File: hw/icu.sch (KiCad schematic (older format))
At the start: 4 parts, among them J101 AMPSEAL_8_POS_VERT_BLACK_SEAL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, J102 AMPSEAL_23_POS_VERT_GRAY_SEAL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

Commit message: implementing icu in CM_6.2.1
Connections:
- net Power supply/GND: now also J101.7 (S), J101.8 (S)
- net Power supply/VIN: no longer J101.6 (S)
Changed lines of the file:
@@
 Connection ~ 1650 2100
 Wire Wire Line
-	1650 2850 1450 2850
-Connection ~ 1650 2400
-Wire Wire Line
-	1450 2250 2850 2250
+	1450 2250 1750 2250
 Wire Wire Line
 	2850 2250 2850 2800
@@
 Wire Wire Line
 	1650 2100 3200 2100
-Wire Wire Line
-	1650 2400 1650 2850
 $Comp
 L icu-rescue:VDD #PWR0101
@@
 Wire Wire Line
 	7200 5750 5950 5750
+Wire Wire Line
+	1450 3000 1750 3000
+Wire Wire Line
+	1750 3000 1750 2250
+Connection ~ 1750 2250
+Wire Wire Line
+	1750 2250 2850 2250
+Wire Wire Line
+	1750 3000 1750 3150
+Wire Wire Line
+	1750 3150 1450 3150
+Connection ~ 1750 3000
 $EndSCHEMATC

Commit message: CM_6.2.1 delivered, first customer machine with CCU, HCU & ICU
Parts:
- removed R101: 120, yageo:0603, symbol yageo:120
- F101: symbol icu-rescue:FUSE_MC36211_350MA -> FUSE_MC36211_350MA
- J101: symbol icu-rescue:AMPSEAL_8_POS_VERT_BLACK_SEALED_1-776276-1 -> AMPSEAL_8_POS_VERT_BLACK_SEALED_1-776276-1
- J102: symbol icu-rescue:AMPSEAL_23_POS_VERT_GRAY_SEALED_1-776228-4 -> AMPSEAL_23_POS_VERT_GRAY_SEALED_1-776228-4
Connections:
- net labels added: 5V_OUT
- net labels removed: VDD_OUT
- wire segments 120 -> 109

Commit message: 050518: Kikepera head prototype first revision, saw not working
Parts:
- F101: symbol FUSE_MC36211_350MA -> icu-rescue:FUSE_MC36211_350MA
- J101: symbol AMPSEAL_8_POS_VERT_BLACK_SEALED_1-776276-1 -> icu-rescue:AMPSEAL_8_POS_VERT_BLACK_SEALED_1-776276-1
- J102: symbol AMPSEAL_23_POS_VERT_GRAY_SEALED_1-776228-4 -> icu-rescue:AMPSEAL_23_POS_VERT_GRAY_SEALED_1-776228-4
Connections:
- wire segments 109 -> 111
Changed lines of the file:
@@
-EESchema Schematic File Version 2
-LIBS:kemet
-LIBS:usevolt
-LIBS:wurth_elektronik_LED
-LIBS:power
-LIBS:yageo
+EESchema Schematic File Version 4
 LIBS:icu-cache
 EELAYER 26 0
@@
 $EndSheet
 $Comp
-L +3V3 #PWR01
+L icu-rescue:+3V3 #PWR01
 U 1 1 57E93CBF
 P 4900 2050
@@
 $EndComp
 $Comp
-L VDD #PWR02
+L icu-rescue:VDD #PWR02
 U 1 1 57E93E22
 P 4400 2050
@@
 $EndComp
 $Comp
-L +5V #PWR03
+L icu-rescue:+5V #PWR03
 U 1 1 589766AF
 P 4650 2050
@@
 	4650 2250 4300 2250
 $Comp
-L AMPSEAL_8_POS_VERT_BLACK_SEALED_1-776276-1 J101
+L icu-rescue:AMPSEAL_8_POS_VERT_BLACK_SEALED_1-776276-1 J101
 U 1 1 5A79A3F3
 P 1350 2100
@@
 $EndComp
 $Comp
-L AMPSEAL_8_POS_VERT_BLACK_SEALED_1-776276-1 J101
+L icu-rescue:AMPSEAL_8_POS_VERT_BLACK_SEALED_1-776276-1 J101
 U 2 1 5A79A545
 P 1350 2250
@@
 $EndComp
 $Comp
-L AMPSEAL_8_POS_VERT_BLACK_SEALED_1-776276-1 J101
+L icu-rescue:AMPSEAL_8_POS_VERT_BLACK_SEALED_1-776276-1 J101
 U 3 1 5A79A8B7
 P 1350 2400
@@
 $EndComp
 $Comp
-L AMPSEAL_8_POS_VERT_BLACK_SEALED_1-776276-1 J101
+L icu-rescue:AMPSEAL_8_POS_VERT_BLACK_SEALED_1-776276-1 J101
 U 4 1 5A79A9C7
 P 1350 2550
@@
 $EndComp
 $Comp
-L AMPSEAL_8_POS_VERT_BLACK_SEALED_1-776276-1 J101
+L icu-rescue:AMPSEAL_8_POS_VERT_BLACK_SEALED_1-776276-1 J101
 U 5 1 5A79AADD
 P 1350 2700
@@
 $EndComp
 $Comp
-L AMPSEAL_8_POS_VERT_BLACK_SEALED_1-776276-1 J101
+L icu-rescue:AMPSEAL_8_POS_VERT_BLACK_SEALED_1-776276-1 J101
 U 6 1 5A79AD45
 P 1350 2850
@@
 $EndComp
 $Comp
-L AMPSEAL_8_POS_VERT_BLACK_SEALED_1-776276-1 J101
+L icu-rescue:AMPSEAL_8_POS_VERT_BLACK_SEALED_1-776276-1 J101
 U 7 1 5A79AE65
 P 1350 3000
@@
 $EndComp
 $Comp
-L AMPSEAL_8_POS_VERT_BLACK_SEALED_1-776276-1 J101
+L icu-rescue:AMPSEAL_8_POS_VERT_BLACK_SEALED_1-776276-1 J101
 U 8 1 5A79AF81
 P 1350 3150
@@
 $EndComp
 Wire Wire Line
-	1450 2100 3200 2100
+	1450 2100 1650 2100
 Wire Wire Line
 	1450 2400 1650 2400
 Wire Wire Line
-	1650 2100 1650 2850
+	1650 2100 1650 2400
 Connection ~ 1650 2100
 Wire Wire Line
@@
 	5800 4550 7200 4550
 $Comp
-L AMPSEAL_23_POS_VERT_GRAY_SEALED_1-776228-4 J102
+L icu-rescue:AMPSEAL_23_POS_VERT_GRAY_SEALED_1-776228-4 J102
 U 1 1 5A7B0192
 P 4600 5050
@@
 $EndComp
 $Comp
-L AMPSEAL_23_POS_VERT_GRAY_SEALED_1-776228-4 J102
+L icu-rescue:AMPSEAL_23_POS_VERT_GRAY_SEALED_1-776228-4 J102
 U 2 1 5A7B0214
 P 4600 5150
@@
 $EndComp
 $Comp
-L AMPSEAL_23_POS_VERT_GRAY_SEALED_1-776228-4 J102
+L icu-rescue:AMPSEAL_23_POS_VERT_GRAY_SEALED_1-776228-4 J102
 U 3 1 5A7B037A
 P 4600 5250
@@
 $EndComp
 $Comp
-L AMPSEAL_23_POS_VERT_GRAY_SEALED_1-776228-4 J102
+L icu-rescue:AMPSEAL_23_POS_VERT_GRAY_SEALED_1-776228-4 J102
 U 4 1 5A7B03F0
 P 4600 5350
@@
 $EndComp
 $Comp
-L AMPSEAL_23_POS_VERT_GRAY_SEALED_1-776228-4 J102
+L icu-rescue:AMPSEAL_23_POS_VERT_GRAY_SEALED_1-776228-4 J102
 U 5 1 5A7B0464
 P 4600 5600
@@
 $EndComp
 $Comp
-L AMPSEAL_23_POS_VERT_GRAY_SEALED_1-776228-4 J102
+L icu-rescue:AMPSEAL_23_POS_VERT_GRAY_SEALED_1-776228-4 J102
 U 6 1 5A7B04DA
 P 4600 6000
@@
 $EndComp
 $Comp
-L AMPSEAL_23_POS_VERT_GRAY_SEALED_1-776228-4 J102
+L icu-rescue:AMPSEAL_23_POS_VERT_GRAY_SEALED_1-776228-4 J102
 U 7 1 5A7B0552
 P 4600 6400
@@
 $EndComp
 $Comp
-L AMPSEAL_23_POS_VERT_GRAY_SEALED_1-776228-4 J102
+L icu-rescue:AMPSEAL_23_POS_VERT_GRAY_SEALED_1-776228-4 J102
 U 8 1 5A7B05CC
 P 4600 6800
@@
 $EndComp
 $Comp
-L AMPSEAL_23_POS_VERT_GRAY_SEALED_1-776228-4 J102
+L icu-rescue:AMPSEAL_23_POS_VERT_GRAY_SEALED_1-776228-4 J102
 U 9 1 5A7B0648
 P 12750 3600
@@
 $EndComp
 $Comp
-L AMPSEAL_23_POS_VERT_GRAY_SEALED_1-776228-4 J102
+L icu-rescue:AMPSEAL_23_POS_VERT_GRAY_SEALED_1-776228-4 J102
 U 10 1 5A7B075E
 P 12750 4200
@@
 $EndComp
 $Comp
-L AMPSEAL_23_POS_VERT_GRAY_SEALED_1-776228-4 J102
+L icu-rescue:AMPSEAL_23_POS_VERT_GRAY_SEALED_1-776228-4 J102
 U 11 1 5A7B07EA
 P 12750 4800
@@
 $EndComp
 $Comp
-L AMPSEAL_23_POS_VERT_GRAY_SEALED_1-776228-4 J102
+L icu-rescue:AMPSEAL_23_POS_VERT_GRAY_SEALED_1-776228-4 J102
 U 12 1 5A7B086C
 P 12750 5400
@@
 $EndComp
 $Comp
-L AMPSEAL_23_POS_VERT_GRAY_SEALED_1-776228-4 J102
+L icu-rescue:AMPSEAL_23_POS_VERT_GRAY_SEALED_1-776228-4 J102
 U 13 1 5A7B08F0
 P 12750 6000
@@
 $EndComp
 $Comp
-L AMPSEAL_23_POS_VERT_GRAY_SEALED_1-776228-4 J102
+L icu-rescue:AMPSEAL_23_POS_VERT_GRAY_SEALED_1-776228-4 J102
 U 14 1 5A7B0976
 P 12750 6600
@@
 $EndComp
 $Comp
-L AMPSEAL_23_POS_VERT_GRAY_SEALED_1-776228-4 J102
+L icu-rescue:AMPSEAL_23_POS_VERT_GRAY_SEALED_1-776228-4 J102
 U 15 1 5A7B09FE
 P 12750 7200
@@
 $EndComp
 $Comp
-L AMPSEAL_23_POS_VERT_GRAY_SEALED_1-776228-4 J102
+L icu-rescue:AMPSEAL_23_POS_VERT_GRAY_SEALED_1-776228-4 J102
 U 16 1 5A7B0A88
 P 12750 3800
@@
 $EndComp
 $Comp
-L AMPSEAL_23_POS_VERT_GRAY_SEALED_1-776228-4 J102
+L icu-rescue:AMPSEAL_23_POS_VERT_GRAY_SEALED_1-776228-4 J102
 U 17 1 5A7B0B14
 P 12750 4400
@@
 $EndComp
 $Comp
-L AMPSEAL_23_POS_VERT_GRAY_SEALED_1-776228-4 J102
+L icu-rescue:AMPSEAL_23_POS_VERT_GRAY_SEALED_1-776228-4 J102
 U 18 1 5A7B0C28
 P 12750 5000
@@
 $EndComp
 $Comp
-L AMPSEAL_23_POS_VERT_GRAY_SEALED_1-776228-4 J102
+L icu-rescue:AMPSEAL_23_POS_VERT_GRAY_SEALED_1-776228-4 J102
 U 19 1 5A7B0CB4
 P 12750 5600
@@
 $EndComp
 $Comp
-L AMPSEAL_23_POS_VERT_GRAY_SEALED_1-776228-4 J102
+L icu-rescue:AMPSEAL_23_POS_VERT_GRAY_SEALED_1-776228-4 J102
 U 20 1 5A7B0DD2
 P 12750 6200
@@
 $EndComp
 $Comp
-L AMPSEAL_23_POS_VERT_GRAY_SEALED_1-776228-4 J102
+L icu-rescue:AMPSEAL_23_POS_VERT_GRAY_SEALED_1-776228-4 J102
 U 21 1 5A7B0F0C
 P 12750 6800
@@
 $EndComp
 $Comp
-L AMPSEAL_23_POS_VERT_GRAY_SEALED_1-776228-4 J102
+L icu-rescue:AMPSEAL_23_POS_VERT_GRAY_SEALED_1-776228-4 J102
 U 22 1 5A7B0FA2
 P 12750 7400
@@
 $EndComp
 $Comp
-L AMPSEAL_23_POS_VERT_GRAY_SEALED_1-776228-4 J102
+L icu-rescue:AMPSEAL_23_POS_VERT_GRAY_SEALED_1-776228-4 J102
 U 23 1 5A7B103A
 P 1700 5850
@@
 	12450 4200 12650 4200
 $Comp
-L FUSE_MC36211_350MA F101
+L icu-rescue:FUSE_MC36211_350MA F101
 U 1 1 5A7D8C08
 P 2400 5850
@@
 5V_OUT
 $Comp
-L +5V #PWR04
+L icu-rescue:+5V #PWR04
 U 1 1 5A7DBD62
 P 2800 5650
@@
 Wire Wire Line
 	6000 6800 7200 6800
+Wire Wire Line
+	1650 2100 3200 2100
+Wire Wire Line
+	1650 2400 1650 2850
 $EndSCHEMATC

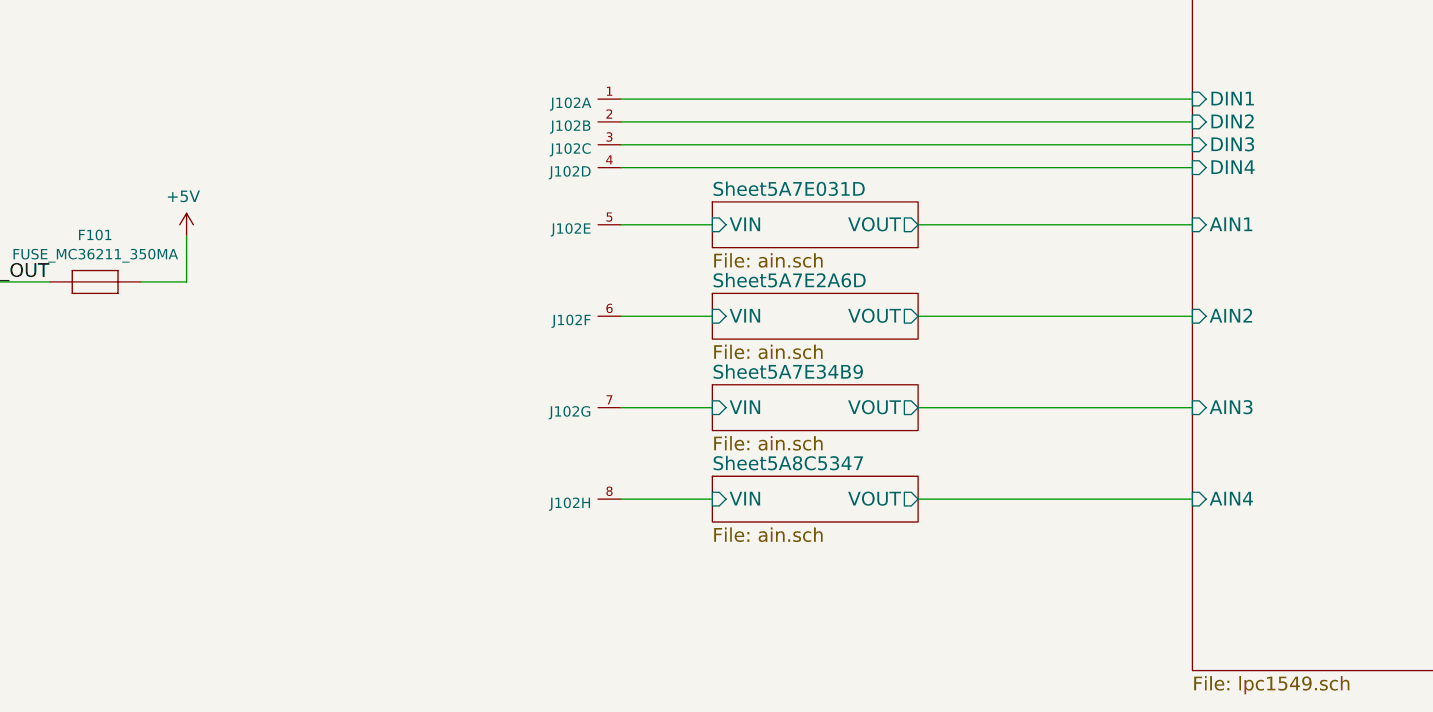
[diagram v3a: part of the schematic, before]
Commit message: analog inputs replaced with digital inputs
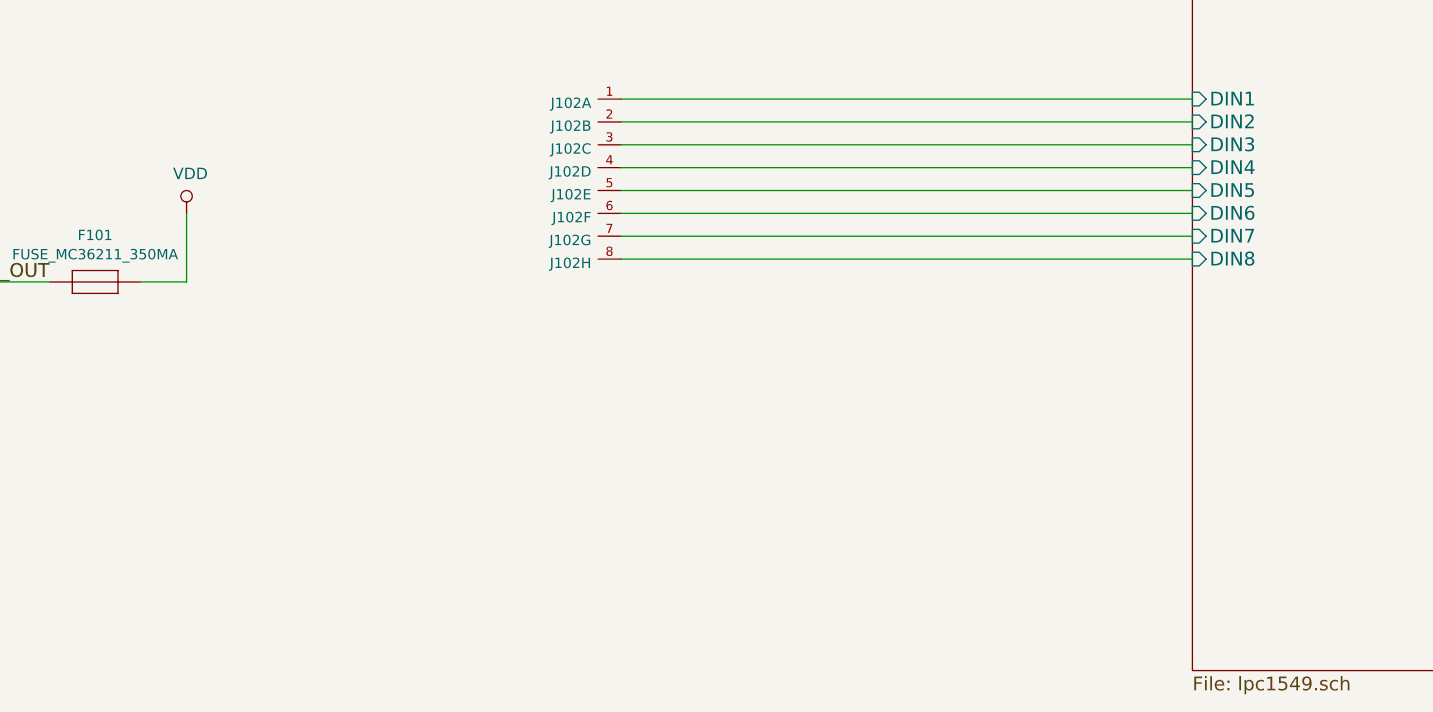
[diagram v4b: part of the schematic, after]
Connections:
- net +5V: no longer F101.P$1
- net VDD: now also F101.P$1
- net Sheet5A7E031D/VIN renamed lpc1549/DIN5
- net Sheet5A7E2A6D/VIN renamed lpc1549/DIN6
- net Sheet5A7E34B9/VIN renamed lpc1549/DIN7
- net Sheet5A8C5347/VIN renamed lpc1549/DIN8
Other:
- moved on the sheet: J102E, J102F, J102G, J102H
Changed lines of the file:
@@
 $Descr A3 16535 11693
 encoding utf-8
-Sheet 1 14
+Sheet 1 10
 Title "ESB version 1"
 Date "2017-02-02"
@@
 L icu-rescue:AMPSEAL_23_POS_VERT_GRAY_SEALED_1-776228-4 J102
 U 5 1 5A7B0464
-P 4600 5600
-F 0 "J102" H 4629 5582 45  0000 L CNN
-F 1 "AMPSEAL_23_POS_VERT_GRAY_SEALED_1-776228-4" H 4600 5600 45  0001 L BNN
-F 2 "usevolt:AMPSEAL_23_POS_776200-1" H 4630 5750 20  0001 C CNN
-F 3 "http://www.mouser.com/ds/2/418/NG_CD_776228_C13-672564.pdf" H 4700 5570 60  0001 C CNN
-F 4 "571-1-776228-4" H 5100 5970 60  0001 C CNN "1st Source Part Number"
-F 5 "1-776228-4" H 4900 5770 60  0001 C CNN "Manufacturer Part Number"
-F 6 "Mouser" H 5000 5870 60  0001 C CNN "1st Source"
-F 7 "TE Connectivity" H 4800 5670 60  0001 C CNN "Manufacturer"
-	5    4600 5600
+P 4600 5450
+F 0 "J102" H 4629 5432 45  0000 L CNN
+F 1 "AMPSEAL_23_POS_VERT_GRAY_SEALED_1-776228-4" H 4600 5450 45  0001 L BNN
+F 2 "usevolt:AMPSEAL_23_POS_776200-1" H 4630 5600 20  0001 C CNN
+F 3 "http://www.mouser.com/ds/2/418/NG_CD_776228_C13-672564.pdf" H 4700 5420 60  0001 C CNN
+F 4 "571-1-776228-4" H 5100 5820 60  0001 C CNN "1st Source Part Number"
+F 5 "1-776228-4" H 4900 5620 60  0001 C CNN "Manufacturer Part Number"
+F 6 "Mouser" H 5000 5720 60  0001 C CNN "1st Source"
+F 7 "TE Connectivity" H 4800 5520 60  0001 C CNN "Manufacturer"
+	5    4600 5450
 	-1   0    0    -1
 $EndComp
@@
 L icu-rescue:AMPSEAL_23_POS_VERT_GRAY_SEALED_1-776228-4 J102
 U 6 1 5A7B04DA
-P 4600 6000
-F 0 "J102" H 4629 5982 45  0000 L CNN
-F 1 "AMPSEAL_23_POS_VERT_GRAY_SEALED_1-776228-4" H 4600 6000 45  0001 L BNN
-F 2 "usevolt:AMPSEAL_23_POS_776200-1" H 4630 6150 20  0001 C CNN
-F 3 "http://www.mouser.com/ds/2/418/NG_CD_776228_C13-672564.pdf" H 4700 5970 60  0001 C CNN
-F 4 "571-1-776228-4" H 5100 6370 60  0001 C CNN "1st Source Part Number"
-F 5 "1-776228-4" H 4900 6170 60  0001 C CNN "Manufacturer Part Number"
-F 6 "Mouser" H 5000 6270 60  0001 C CNN "1st Source"
-F 7 "TE Connectivity" H 4800 6070 60  0001 C CNN "Manufacturer"
-	6    4600 6000
+P 4600 5550
+F 0 "J102" H 4629 5532 45  0000 L CNN
+F 1 "AMPSEAL_23_POS_VERT_GRAY_SEALED_1-776228-4" H 4600 5550 45  0001 L BNN
+F 2 "usevolt:AMPSEAL_23_POS_776200-1" H 4630 5700 20  0001 C CNN
+F 3 "http://www.mouser.com/ds/2/418/NG_CD_776228_C13-672564.pdf" H 4700 5520 60  0001 C CNN
+F 4 "571-1-776228-4" H 5100 5920 60  0001 C CNN "1st Source Part Number"
+F 5 "1-776228-4" H 4900 5720 60  0001 C CNN "Manufacturer Part Number"
+F 6 "Mouser" H 5000 5820 60  0001 C CNN "1st Source"
+F 7 "TE Connectivity" H 4800 5620 60  0001 C CNN "Manufacturer"
+	6    4600 5550
 	-1   0    0    -1
 $EndComp
@@
 L icu-rescue:AMPSEAL_23_POS_VERT_GRAY_SEALED_1-776228-4 J102
 U 7 1 5A7B0552
-P 4600 6400
-F 0 "J102" H 4629 6382 45  0000 L CNN
-F 1 "AMPSEAL_23_POS_VERT_GRAY_SEALED_1-776228-4" H 4600 6400 45  0001 L BNN
-F 2 "usevolt:AMPSEAL_23_POS_776200-1" H 4630 6550 20  0001 C CNN
-F 3 "http://www.mouser.com/ds/2/418/NG_CD_776228_C13-672564.pdf" H 4700 6370 60  0001 C CNN
-F 4 "571-1-776228-4" H 5100 6770 60  0001 C CNN "1st Source Part Number"
-F 5 "1-776228-4" H 4900 6570 60  0001 C CNN "Manufacturer Part Number"
-F 6 "Mouser" H 5000 6670 60  0001 C CNN "1st Source"
-F 7 "TE Connectivity" H 4800 6470 60  0001 C CNN "Manufacturer"
-	7    4600 6400
+P 4600 5650
+F 0 "J102" H 4629 5632 45  0000 L CNN
+F 1 "AMPSEAL_23_POS_VERT_GRAY_SEALED_1-776228-4" H 4600 5650 45  0001 L BNN
+F 2 "usevolt:AMPSEAL_23_POS_776200-1" H 4630 5800 20  0001 C CNN
+F 3 "http://www.mouser.com/ds/2/418/NG_CD_776228_C13-672564.pdf" H 4700 5620 60  0001 C CNN
+F 4 "571-1-776228-4" H 5100 6020 60  0001 C CNN "1st Source Part Number"
+F 5 "1-776228-4" H 4900 5820 60  0001 C CNN "Manufacturer Part Number"
+F 6 "Mouser" H 5000 5920 60  0001 C CNN "1st Source"
+F 7 "TE Connectivity" H 4800 5720 60  0001 C CNN "Manufacturer"
+	7    4600 5650
 	-1   0    0    -1
 $EndComp
@@
 L icu-rescue:AMPSEAL_23_POS_VERT_GRAY_SEALED_1-776228-4 J102
 U 8 1 5A7B05CC
-P 4600 6800
-F 0 "J102" H 4629 6782 45  0000 L CNN
-F 1 "AMPSEAL_23_POS_VERT_GRAY_SEALED_1-776228-4" H 4600 6800 45  0001 L BNN
-F 2 "usevolt:AMPSEAL_23_POS_776200-1" H 4630 6950 20  0001 C CNN
-F 3 "http://www.mouser.com/ds/2/418/NG_CD_776228_C13-672564.pdf" H 4700 6770 60  0001 C CNN
-F 4 "571-1-776228-4" H 5100 7170 60  0001 C CNN "1st Source Part Number"
-F 5 "1-776228-4" H 4900 6970 60  0001 C CNN "Manufacturer Part Number"
-F 6 "Mouser" H 5000 7070 60  0001 C CNN "1st Source"
-F 7 "TE Connectivity" H 4800 6870 60  0001 C CNN "Manufacturer"
-	8    4600 6800
+P 4600 5750
+F 0 "J102" H 4629 5732 45  0000 L CNN
+F 1 "AMPSEAL_23_POS_VERT_GRAY_SEALED_1-776228-4" H 4600 5750 45  0001 L BNN
+F 2 "usevolt:AMPSEAL_23_POS_776200-1" H 4630 5900 20  0001 C CNN
+F 3 "http://www.mouser.com/ds/2/418/NG_CD_776228_C13-672564.pdf" H 4700 5720 60  0001 C CNN
+F 4 "571-1-776228-4" H 5100 6120 60  0001 C CNN "1st Source Part Number"
+F 5 "1-776228-4" H 4900 5920 60  0001 C CNN "Manufacturer Part Number"
+F 6 "Mouser" H 5000 6020 60  0001 C CNN "1st Source"
+F 7 "TE Connectivity" H 4800 5820 60  0001 C CNN "Manufacturer"
+	8    4600 5750
 	-1   0    0    -1
 $EndComp
@@
 F26 "DIN2" I L 7200 5150 60
 F27 "DIN3" I L 7200 5250 60
-F28 "AIN1" I L 7200 5600 60
-F29 "AIN2" I L 7200 6000 60
-F30 "AIN3" I L 7200 6400 60
-F31 "AIN4" I L 7200 6800 60
-F32 "DIN4" I L 7200 5350 60
+F28 "DIN4" I L 7200 5350 60
+F29 "DIN5" I L 7200 5450 60
+F30 "DIN6" I L 7200 5550 60
+F31 "DIN7" I L 7200 5650 60
+F32 "DIN8" I L 7200 5750 60
 $EndSheet
 Wire Wire Line
@@
 Text Label 2200 5850 2    60   ~ 0
 5V_OUT
-$Comp
-L icu-rescue:+5V #PWR04
-U 1 1 5A7DBD62
-P 2800 5650
-F 0 "#PWR04" H 2800 5500 50  0001 C CNN
-F 1 "+5V" H 2815 5823 50  0000 C CNN
-F 2 "" H 2800 5650 50  0000 C CNN
-F 3 "" H 2800 5650 50  0000 C CNN
-	1    2800 5650
-	-1   0    0    -1
-$EndComp
-Wire Wire Line
-	2800 5650 2800 5850
 Wire Wire Line
 	2800 5850 2600 5850
-$Sheet
-S 5100 5500 900  200
-U 5A7E031E
-F0 "Sheet5A7E031D" 60
-F1 "ain.sch" 60
-F2 "VOUT" O R 6000 5600 60
-F3 "VIN" I L 5100 5600 60
-$EndSheet
-$Sheet
-S 5100 5900 900  200
-U 5A7E2A6E
-F0 "Sheet5A7E2A6D" 60
-F1 "ain.sch" 60
-F2 "VOUT" O R 6000 6000 60
-F3 "VIN" I L 5100 6000 60
-$EndSheet
-$Sheet
-S 5100 6300 900  200
-U 5A7E34BA
-F0 "Sheet5A7E34B9" 60
-F1 "ain.sch" 60
-F2 "VOUT" O R 6000 6400 60
-F3 "VIN" I L 5100 6400 60
-$EndSheet
-Wire Wire Line
-	4700 5600 5100 5600
-Wire Wire Line
-	5100 6000 4700 6000
-Wire Wire Line
-	4700 6400 5100 6400
 Wire Wire Line
 	4700 5050 7200 5050
@@
 	4700 5250 7200 5250
 Wire Wire Line
-	7200 6400 6000 6400
-Wire Wire Line
-	6000 6000 7200 6000
-Wire Wire Line
-	7200 5600 6000 5600
-$Sheet
-S 5100 6700 900  200
-U 5A8C5348
-F0 "Sheet5A8C5347" 60
-F1 "ain.sch" 60
-F2 "VOUT" O R 6000 6800 60
-F3 "VIN" I L 5100 6800 60
-$EndSheet
-Wire Wire Line
-	5100 6800 4700 6800
-Wire Wire Line
 	7200 5350 4700 5350
 Wire Wire Line
-	6000 6800 7200 6800
-Wire Wire Line
 	1650 2100 3200 2100
 Wire Wire Line
 	1650 2400 1650 2850
+$Comp
+L icu-rescue:VDD #PWR0101
+U 1 1 5B1D8945
+P 2800 5550
+F 0 "#PWR0101" H 2800 5400 50  0001 C CNN
+F 1 "VDD" H 2817 5723 50  0000 C CNN
+F 2 "" H 2800 5550 50  0000 C CNN
+F 3 "" H 2800 5550 50  0000 C CNN
+	1    2800 5550
+	1    0    0    -1
+$EndComp
+Wire Wire Line
+	2800 5550 2800 5850
+Wire Wire Line
+	4700 5450 7200 5450
+Wire Wire Line
+	4700 5550 7200 5550
+Wire Wire Line
+	4700 5650 7200 5650
+Wire Wire Line
+	4700 5750 7200 5750
 $EndSCHEMATC
